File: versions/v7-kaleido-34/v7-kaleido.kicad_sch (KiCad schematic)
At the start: 139 parts, among them J1 USB_C_Receptacle_USB2.0, J10 AXT-310124, J11 THD2528-11SD-GF, J12 SM04B-SRSS-TB_LF__SN_, J2 EXTENSION_HEADER, J3 USB_HDR, J4 Conn_01x08_Pin, J5 CONN_BAT, J6 FH34SRJ-6S-0.5SH_99_, J7 ESP_HDR, J8 ESP_XTR_HDR, J9 Conn_01x08_Pin, Q1 AO3401A, Q3 MMBT3904, Q4 MMBT3904, U1 RT9080-33GJ5, U10 ED060XC5, U11 TP4056, U12 RY3730, U2 PCA9535PW, U3 TPS651851RSLR, U4 USBLC6-2P6, U5 XC6206PxxxMR, U6 RY3730, U7 PCF8563T, U8 ESP32-S3-WROOM-1, U9 CH340C, Y1 32.768K

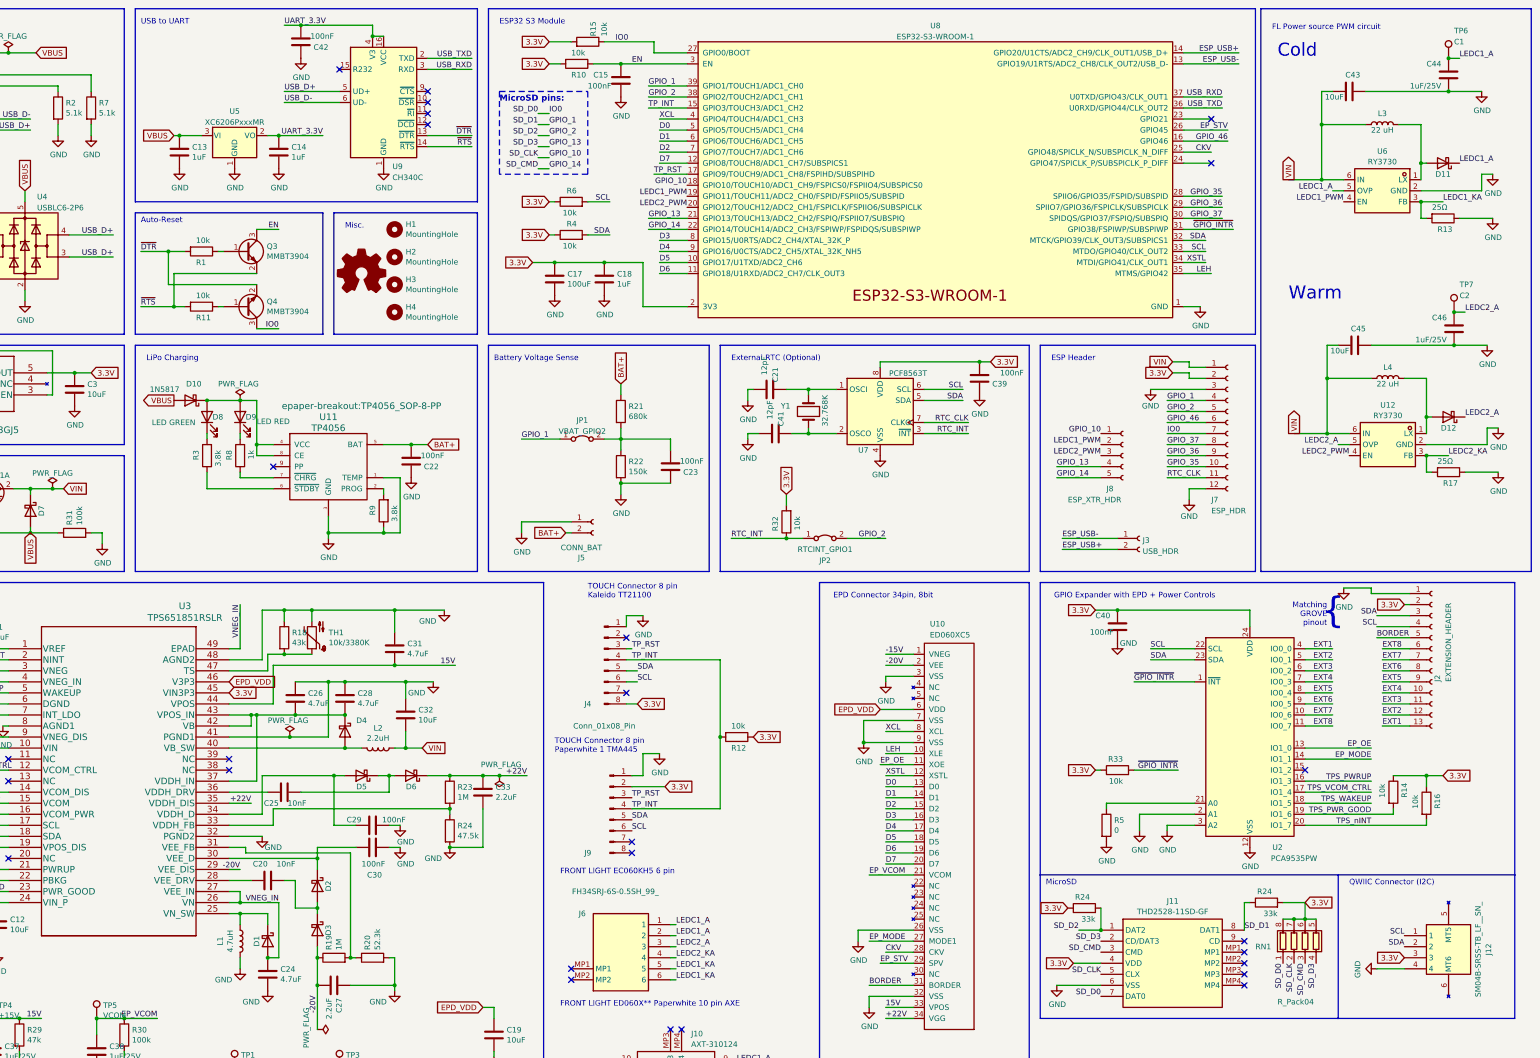
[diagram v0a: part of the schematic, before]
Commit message: Add kindle 34 pins versions (RAW)
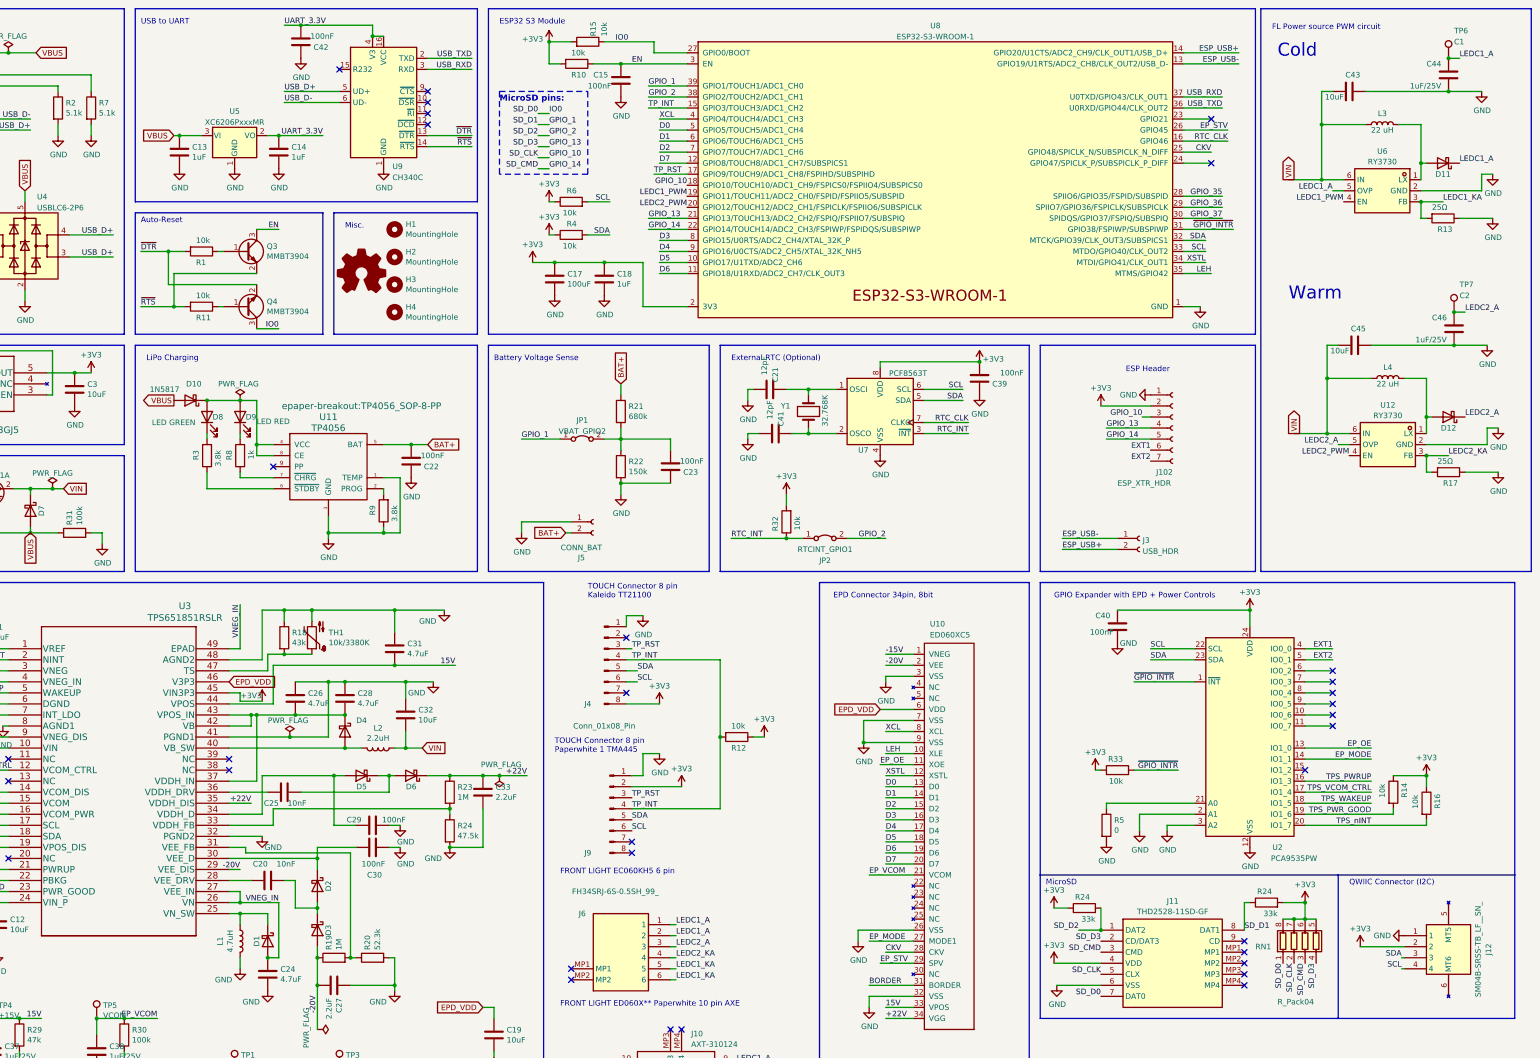
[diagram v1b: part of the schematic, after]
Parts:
- removed J2: EXTENSION_HEADER, Connector_PinHeader_2.54mm:PinHeader_1x13_P2.54mm_Vertical, symbol Connector:Conn_01x13_Socket
- removed J7: ESP_HDR, Connector_PinHeader_2.54mm:PinHeader_1x12_P2.54mm_Vertical, symbol Connector:Conn_01x12_Socket
- removed J8: ESP_XTR_HDR, Connector_PinHeader_2.54mm:PinHeader_1x05_P2.54mm_Vertical, symbol Connector:Conn_01x05_Socket
- added J102: ESP_XTR_HDR, Connector_PinHeader_2.54mm:PinHeader_1x07_P2.54mm_Vertical, symbol Connector:Conn_01x07_Socket
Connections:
- net GPIO_46 is gone; now on net RTC_CLK: U8.16 (GPIO46)
- net EXT1: now also J102.6 (Pin_6)
- net EXT2: now also J102.7 (Pin_7)
- net GND: now also J12.1, J102.1 (Pin_1); no longer J12.4
- net GPIO_10: now also J102.3 (Pin_3)
- net GPIO_13: now also J102.4 (Pin_4)
- net GPIO_14: now also J102.5 (Pin_5)
- net SCL: now also J12.4; no longer J12.1
- net SDA: now also J12.3; no longer J12.2
- net 3.3V renamed +3V3
- net +3V3: now also J12.2, J102.2 (Pin_2); no longer J12.3
- net EXT3: no longer names the net of U2.6 (IO0_2)
- net EXT4: no longer names the net of U2.7 (IO0_3)
- net EXT5: no longer names the net of U2.8 (IO0_4)
- net EXT6: no longer names the net of U2.9 (IO0_5)
- net EXT7: no longer names the net of U2.10 (IO0_6)
- net EXT8: no longer names the net of U2.11 (IO0_7)
- no-connect marks 38 -> 44
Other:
- note removed: "Matching GROVE pinout"
- note removed: "{"
